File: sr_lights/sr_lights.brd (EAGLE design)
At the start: 78.4 x 64.8 mm, 33 parts, among them T1 BC847, T2 BC847, T3 BC847, T4 BC847, T5 BC847, T6 BC847, T7 BC847, T8 BC847

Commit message: DRC: Fixes and approves
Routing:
- net SI0: track 62.6 -> 68.2 mm
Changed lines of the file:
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@@
 <layer number="18" name="Vias" color="2" fill="1" visible="yes" active="yes"/>
 <layer number="19" name="Unrouted" color="6" fill="1" visible="yes" active="yes"/>
-<layer number="20" name="Dimension" color="15" fill="1" visible="yes" active="yes"/>
-<layer number="21" name="tPlace" color="7" fill="1" visible="yes" active="yes"/>
-<layer number="22" name="bPlace" color="7" fill="1" visible="yes" active="yes"/>
-<layer number="23" name="tOrigins" color="15" fill="1" visible="yes" active="yes"/>
-<layer number="24" name="bOrigins" color="15" fill="1" visible="yes" active="yes"/>
-<layer number="25" name="tNames" color="7" fill="1" visible="yes" active="yes"/>
-<layer number="26" name="bNames" color="7" fill="1" visible="yes" active="yes"/>
-<layer number="27" name="tValues" color="7" fill="1" visible="yes" active="yes"/>
-<layer number="28" name="bValues" color="7" fill="1" visible="yes" active="yes"/>
-<layer number="29" name="tStop" color="7" fill="3" visible="yes" active="yes"/>
-<layer number="30" name="bStop" color="7" fill="6" visible="yes" active="yes"/>
-<layer number="31" name="tCream" color="7" fill="4" visible="yes" active="yes"/>
-<layer number="32" name="bCream" color="7" fill="5" visible="yes" active="yes"/>
-<layer number="33" name="tFinish" color="6" fill="3" visible="yes" active="yes"/>
-<layer number="34" name="bFinish" color="6" fill="6" visible="yes" active="yes"/>
-<layer number="35" name="tGlue" color="7" fill="4" visible="yes" active="yes"/>
-<layer number="36" name="bGlue" color="7" fill="5" visible="yes" active="yes"/>
-<layer number="37" name="tTest" color="7" fill="1" visible="yes" active="yes"/>
-<layer number="38" name="bTest" color="7" fill="1" visible="yes" active="yes"/>
-<layer number="39" name="tKeepout" color="4" fill="11" visible="yes" active="yes"/>
-<layer number="40" name="bKeepout" color="1" fill="11" visible="yes" active="yes"/>
-<layer number="41" name="tRestrict" color="4" fill="10" visible="yes" active="yes"/>
-<layer number="42" name="bRestrict" color="1" fill="10" visible="yes" active="yes"/>
-<layer number="43" name="vRestrict" color="2" fill="10" visible="yes" active="yes"/>
-<layer number="44" name="Drills" color="7" fill="1" visible="yes" active="yes"/>
-<layer number="45" name="Holes" color="7" fill="1" visible="yes" active="yes"/>
-<layer number="46" name="Milling" color="3" fill="1" visible="yes" active="yes"/>
-<layer number="47" name="Measures" color="7" fill="1" visible="yes" active="yes"/>
-<layer number="48" name="Document" color="7" fill="1" visible="yes" active="yes"/>
-<layer number="49" name="Reference" color="7" fill="1" visible="yes" active="yes"/>
-<layer number="51" name="tDocu" color="7" fill="1" visible="yes" active="yes"/>
-<layer number="52" name="bDocu" color="7" fill="1" visible="yes" active="yes"/>
+<layer number="20" name="Dimension" color="15" fill="1" visible="no" active="yes"/>
+<layer number="21" name="tPlace" color="7" fill="1" visible="no" active="yes"/>
+<layer number="22" name="bPlace" color="7" fill="1" visible="no" active="yes"/>
+<layer number="23" name="tOrigins" color="15" fill="1" visible="no" active="yes"/>
+<layer number="24" name="bOrigins" color="15" fill="1" visible="no" active="yes"/>
+<layer number="25" name="tNames" color="7" fill="1" visible="no" active="yes"/>
+<layer number="26" name="bNames" color="7" fill="1" visible="no" active="yes"/>
+<layer number="27" name="tValues" color="7" fill="1" visible="no" active="yes"/>
+<layer number="28" name="bValues" color="7" fill="1" visible="no" active="yes"/>
+<layer number="29" name="tStop" color="7" fill="3" visible="no" active="yes"/>
+<layer number="30" name="bStop" color="7" fill="6" visible="no" active="yes"/>
+<layer number="31" name="tCream" color="7" fill="4" visible="no" active="yes"/>
+<layer number="32" name="bCream" color="7" fill="5" visible="no" active="yes"/>
+<layer number="33" name="tFinish" color="6" fill="3" visible="no" active="yes"/>
+<layer number="34" name="bFinish" color="6" fill="6" visible="no" active="yes"/>
+<layer number="35" name="tGlue" color="7" fill="4" visible="no" active="yes"/>
+<layer number="36" name="bGlue" color="7" fill="5" visible="no" active="yes"/>
+<layer number="37" name="tTest" color="7" fill="1" visible="no" active="yes"/>
+<layer number="38" name="bTest" color="7" fill="1" visible="no" active="yes"/>
+<layer number="39" name="tKeepout" color="4" fill="11" visible="no" active="yes"/>
+<layer number="40" name="bKeepout" color="1" fill="11" visible="no" active="yes"/>
+<layer number="41" name="tRestrict" color="4" fill="10" visible="no" active="yes"/>
+<layer number="42" name="bRestrict" color="1" fill="10" visible="no" active="yes"/>
+<layer number="43" name="vRestrict" color="2" fill="10" visible="no" active="yes"/>
+<layer number="44" name="Drills" color="7" fill="1" visible="no" active="yes"/>
+<layer number="45" name="Holes" color="7" fill="1" visible="no" active="yes"/>
+<layer number="46" name="Milling" color="3" fill="1" visible="no" active="yes"/>
+<layer number="47" name="Measures" color="7" fill="1" visible="no" active="yes"/>
+<layer number="48" name="Document" color="7" fill="1" visible="no" active="yes"/>
+<layer number="49" name="Reference" color="7" fill="1" visible="no" active="yes"/>
+<layer number="51" name="tDocu" color="7" fill="1" visible="no" active="yes"/>
+<layer number="52" name="bDocu" color="7" fill="1" visible="no" active="yes"/>
 <layer number="90" name="Modules" color="5" fill="1" visible="no" active="no"/>
 <layer number="91" name="Nets" color="2" fill="1" visible="no" active="no"/>
@@
 <via x="45.72" y="33.02" extent="1-16" drill="0.8" shape="square"/>
 <via x="50.8" y="33.02" extent="1-16" drill="0.8" shape="square"/>
-<wire x1="10.16" y1="33.02" x2="15.24" y2="33.02" width="0.4064" layer="1"/>
-<wire x1="15.24" y1="33.02" x2="20.32" y2="33.02" width="0.4064" layer="1"/>
-<wire x1="20.32" y1="33.02" x2="25.4" y2="33.02" width="0.4064" layer="1"/>
-<wire x1="25.4" y1="33.02" x2="30.48" y2="33.02" width="0.4064" layer="1"/>
-<wire x1="30.48" y1="33.02" x2="35.56" y2="33.02" width="0.4064" layer="1"/>
-<wire x1="35.56" y1="33.02" x2="40.64" y2="33.02" width="0.4064" layer="1"/>
-<wire x1="40.64" y1="33.02" x2="45.72" y2="33.02" width="0.4064" layer="1"/>
-<wire x1="45.72" y1="33.02" x2="50.8" y2="33.02" width="0.4064" layer="1"/>
+<wire x1="10.16" y1="33.02" x2="15.24" y2="33.02" width="0.508" layer="1"/>
+<wire x1="15.24" y1="33.02" x2="20.32" y2="33.02" width="0.508" layer="1"/>
+<wire x1="20.32" y1="33.02" x2="25.4" y2="33.02" width="0.508" layer="1"/>
+<wire x1="25.4" y1="33.02" x2="30.48" y2="33.02" width="0.508" layer="1"/>
+<wire x1="30.48" y1="33.02" x2="35.56" y2="33.02" width="0.508" layer="1"/>
+<wire x1="35.56" y1="33.02" x2="40.64" y2="33.02" width="0.508" layer="1"/>
+<wire x1="40.64" y1="33.02" x2="45.72" y2="33.02" width="0.508" layer="1"/>
+<wire x1="45.72" y1="33.02" x2="50.8" y2="33.02" width="0.508" layer="1"/>
 <wire x1="42.53865" y1="46.9392" x2="42.00525" y2="46.9392" width="0.381" layer="16"/>
 <wire x1="42.00525" y1="46.9392" x2="41.91" y2="46.99" width="0.381" layer="16"/>
@@
 <wire x1="51.181" y1="10.795" x2="49.276" y2="8.89" width="0.508" layer="16"/>
 <wire x1="51.308" y1="28.194" x2="51.308" y2="10.922" width="0.508" layer="16"/>
-<wire x1="50.546" y1="28.956" x2="51.308" y2="28.194" width="0.508" layer="16"/>
 <wire x1="50.546" y1="28.956" x2="50.48" y2="29.04" width="0.508" layer="16"/>
 <wire x1="6.35" y1="36.322" x2="6.35" y2="54.61" width="0.508" layer="16"/>
-<wire x1="9.652" y1="33.02" x2="6.35" y2="36.322" width="0.508" layer="16"/>
 <wire x1="9.652" y1="33.02" x2="10.16" y2="33.02" width="0.508" layer="16"/>
 <wire x1="68.58" y1="8.382" x2="68.58" y2="8.89" width="0.508" layer="16"/>
@@
 <wire x1="68.58" y1="55.88" x2="68.58" y2="56.388" width="0.508" layer="16"/>
 <wire x1="31.75" y1="55.118" x2="31.75" y2="54.61" width="0.508" layer="16"/>
+<wire x1="50.546" y1="28.956" x2="51.308" y2="28.194" width="0.508" layer="16"/>
+<wire x1="9.652" y1="33.02" x2="6.35" y2="36.322" width="0.508" layer="16"/>
 </signal>
 <signal name="VCC1" class="2">
@@
 <contactref element="IC_R1" pad="14"/>
 <contactref element="LOGIC_IN" pad="6"/>
-<wire x1="30.226" y1="53.594" x2="29.21" y2="54.61" width="0.508" layer="16"/>
-<wire x1="30.226" y1="53.34" x2="30.226" y2="53.594" width="0.508" layer="16"/>
-<wire x1="34.29" y1="49.276" x2="30.226" y2="53.34" width="0.508" layer="16"/>
-<wire x1="42.418" y1="49.276" x2="34.29" y2="49.276" width="0.508" layer="16"/>
-<wire x1="58.42" y1="33.274" x2="42.418" y2="49.276" width="0.508" layer="16"/>
-<wire x1="58.42" y1="8.89" x2="58.42" y2="33.274" width="0.508" layer="16"/>
+<wire x1="58.42" y1="8.89" x2="58.42" y2="40.64" width="0.508" layer="16"/>
+<wire x1="29.21" y1="54.61" x2="29.21" y2="52.07" width="0.508" layer="16"/>
+<wire x1="29.21" y1="52.07" x2="30.48" y2="50.8" width="0.508" layer="16"/>
+<wire x1="30.48" y1="50.8" x2="48.26" y2="50.8" width="0.508" layer="16"/>
+<wire x1="48.26" y1="50.8" x2="58.42" y2="40.64" width="0.508" layer="16"/>
 </signal>
 <signal name="SCLR">
@@
 </signal>
 </signals>
+<errors>
+</errors>
 </board>
 </drawing>

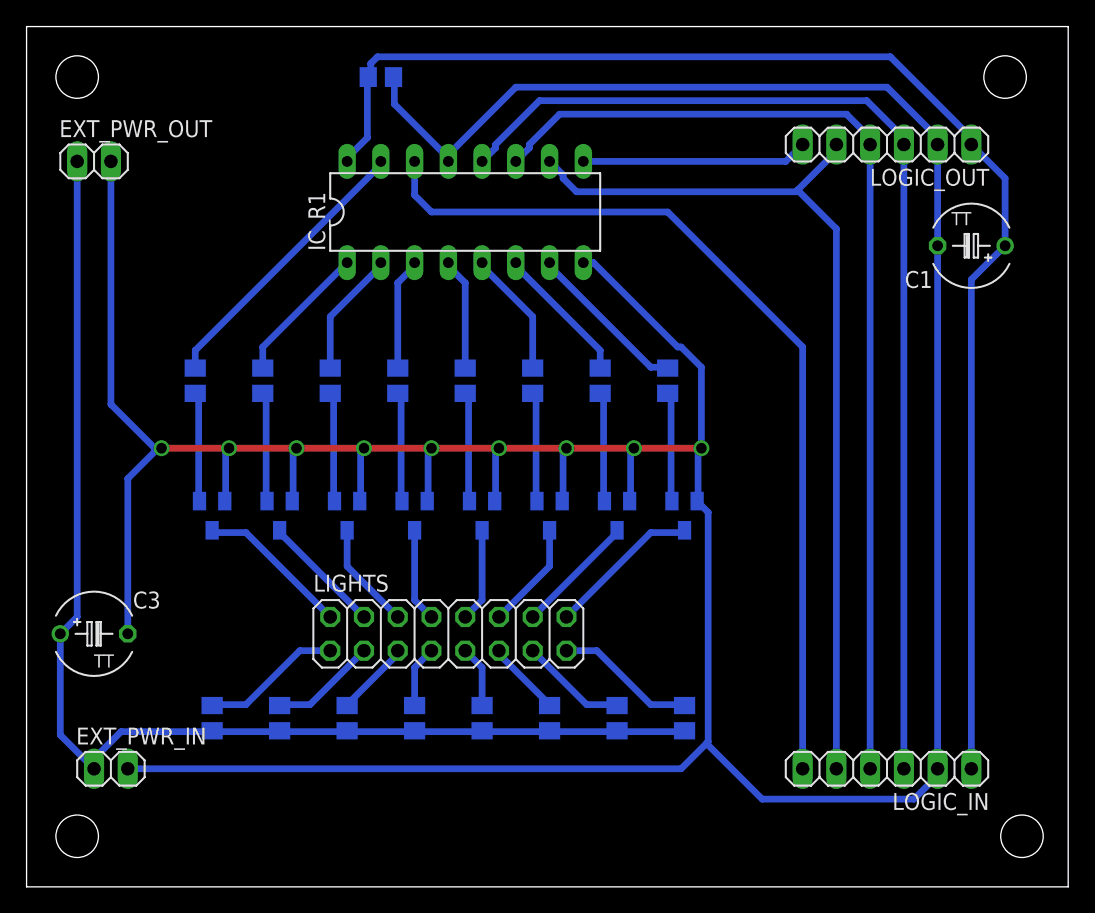
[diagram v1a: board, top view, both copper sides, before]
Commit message: Routes and positions - aligned PWR connectors, top right hole - moved C3 capacitor - updated routes - approved some DRC errors (short route segments near pads)
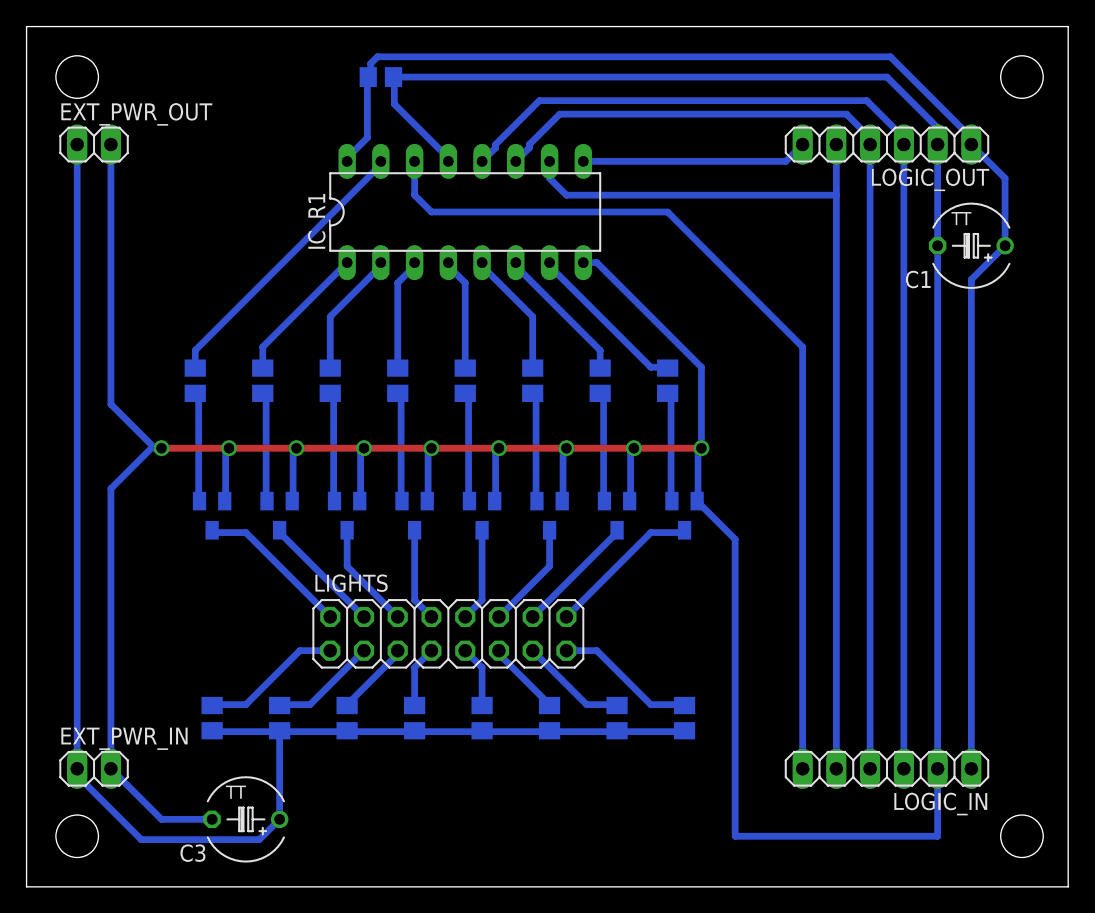
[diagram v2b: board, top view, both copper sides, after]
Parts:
- moved C3 18.1 mm to (16.5, 5.08), turned to 180 degrees
- moved EXT_PWR_OUT 1.27 mm to (5.08, 55.9)
- moved EXT_PWR_IN 1.27 mm to (5.08, 8.89)
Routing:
- net VCC2: track 94.0 -> 108.1 mm
- net GND: track 310.7 -> 297.9 mm
- net SCLR: track 69.2 -> 70.4 mm
